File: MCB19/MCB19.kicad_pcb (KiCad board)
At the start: 2 copper layers, 88 parts, among them J401 USART, J402 DISABLE, J601 RJ45, J602 RJ45, J611 +BATT, J612 GND, J613 VBAT+, J614 VBAT-, Q601 IRFP260N, Q602 IRFP260N, U201 MCP2551-I/SN, U202 MCP2515-xSO, U401 ATMEGA328P-PU, U501 LM7805, U601 LM5104MNOPB, U602 INA211_DCK_6, U603 LM324, Y201 16MHz, Y401 16MHz

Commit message: Mudança nas trilhas para melhor funcionamento
Detalhes finais para a fabricação
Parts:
- removed C405: 100nF, Capacitor_SMD:C_0805_2012Metric_Pad1.15x1.40mm_HandSolder
- added R411: 100, Resistor_SMD:R_0805_2012Metric_Pad1.15x1.40mm_HandSolder, B.Cu at (158.8, 105.0)
- moved U602 2.51 mm to (90.7, 90.8)
- moved R401 2.09 mm to (160.9, 107.5)
- moved R610 1.69 mm to (86.8, 89.7), turned to 180 degrees
- moved R609 1.63 mm to (86.8, 92.2)
- moved TP209 0.49 mm to (166.4, 65.5)
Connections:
- J401 pad 4: Net-(C405-Pad2) -> /MCU/RESET
- U401 pad 1: /MCU/RESET -> Net-(R411-Pad2)
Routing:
- net GND: track 306.1 -> 332.5 mm, vias 20 -> 30
- net Net-(C405-Pad2): track 6.59 -> 0.00 mm
- net /MCU/RESET: track 12.1 -> 16.9 mm
- net Net-(R411-Pad2): track 0.00 -> 4.12 mm
- net Net-(J613-Pad1): track 67.9 -> 65.1 mm
- net Net-(R609-Pad2): track 4.69 -> 7.00 mm
- net /MCU/INALLL: track 71.7 -> 73.6 mm
- net Net-(C603-Pad1): track 29.0 -> 27.3 mm
- net Net-(C601-Pad2): track 108.6 -> 109.9 mm
- net +5V: track 339.9 -> 340.5 mm
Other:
- net class Shunt added: clearance 0.127, trace_width 0.508, via_dia 1.5, via_drill 0.8

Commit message: Final!!!
Pronto para fabricar
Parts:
- moved C606 34.3 mm to (94.1, 63.1), turned to 0 degrees
- moved R607 32.1 mm to (89.7, 63.1), turned to 180 degrees
- moved D604 29.4 mm to (91.5, 65.8), turned to 180 degrees
- moved U603 22.4 mm to (77.3, 116.0)
- moved R609 21.9 mm to (75.0, 110.7)
- moved R610 21.7 mm to (78.2, 109.7), turned to 270 degrees
- moved C607 7.16 mm to (109.5, 99.6)
- moved D605 7.16 mm to (106.9, 97.0)
- moved R608 7.16 mm to (109.5, 95.2)
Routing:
- net GND: track 332.5 -> 242.7 mm
- net Net-(J613-Pad1): track 65.1 -> 5.54 mm
- net Net-(C601-Pad2): track 109.9 -> 130.8 mm
- net +BATT: track 84.9 -> 71.3 mm
- net +5V: track 340.5 -> 350.1 mm, vias 8 -> 10
- net /MCU/INALLL: track 73.6 -> 79.6 mm
- net /driver/LM324A: track 80.8 -> 75.7 mm, vias 2 -> 0
- net Net-(R609-Pad2): track 7.00 -> 4.96 mm
- added copper zone on B.Cu, net Net-(J613-Pad1)

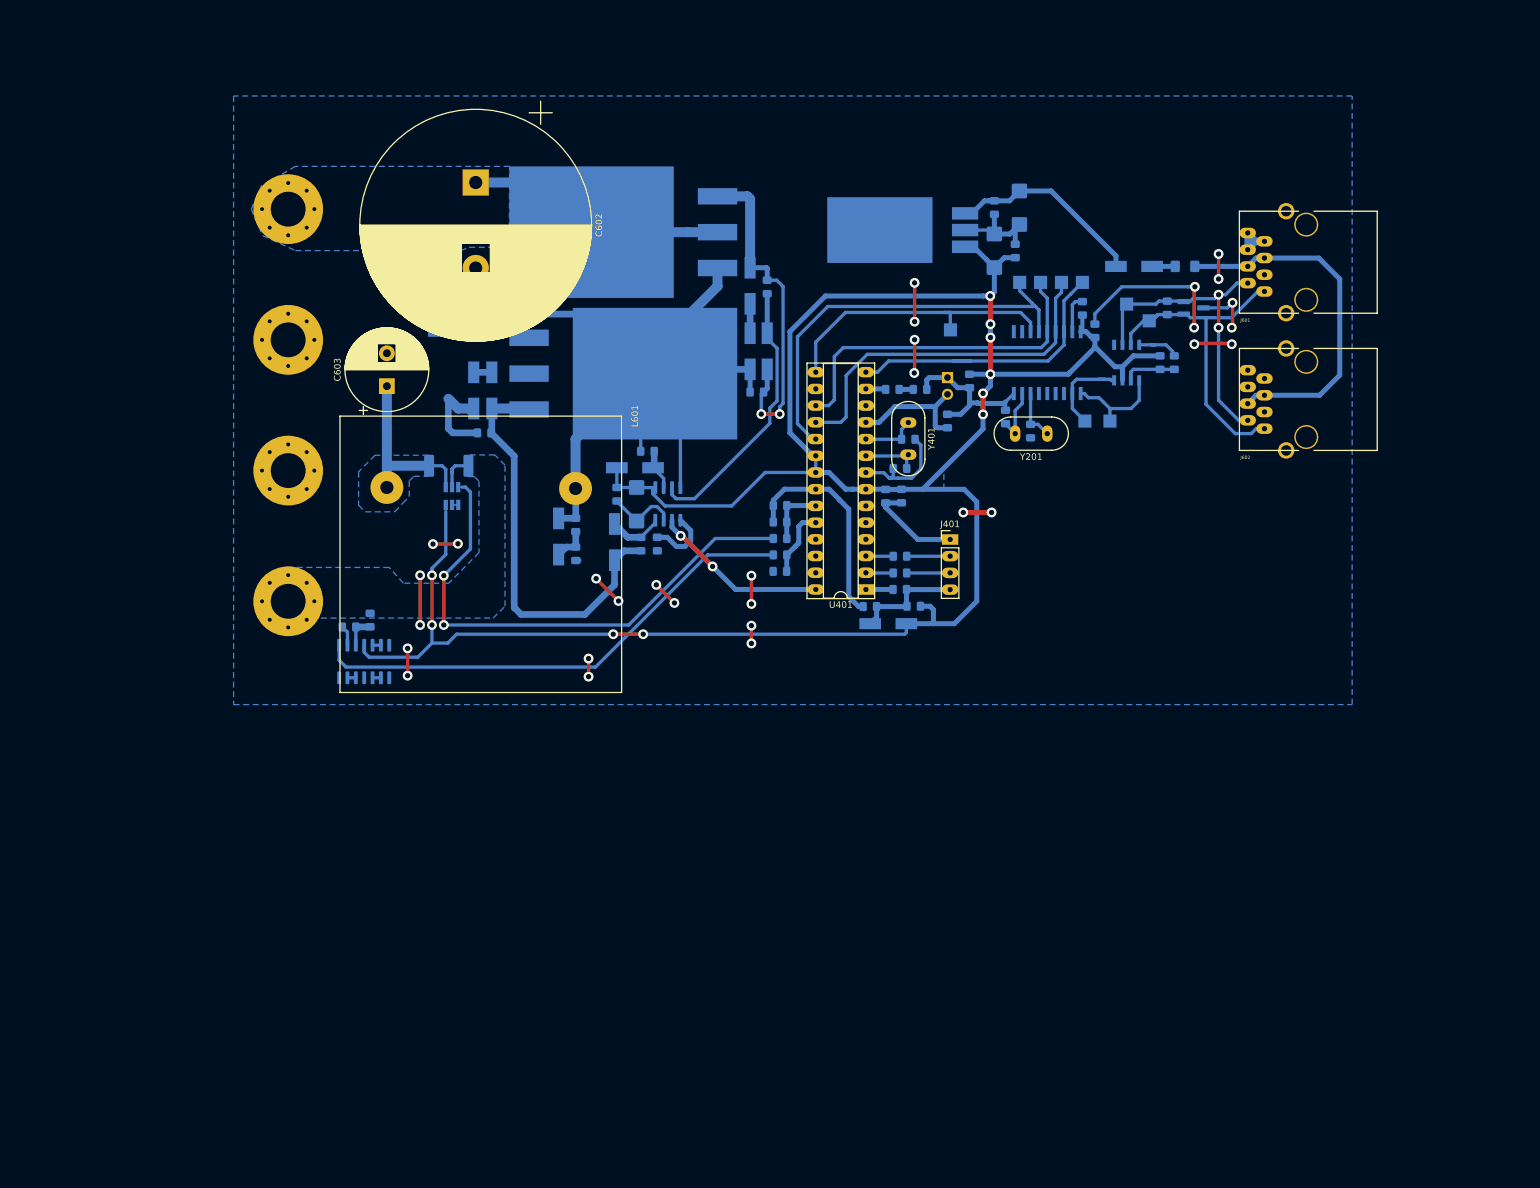
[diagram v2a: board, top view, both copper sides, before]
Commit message: Capacitor corrigido
Havia um capacitor com medidas erradas, que já foram corrigidas.
Para o protótipo já desenvolvido, não ha problemas pois há espaço para a correção.
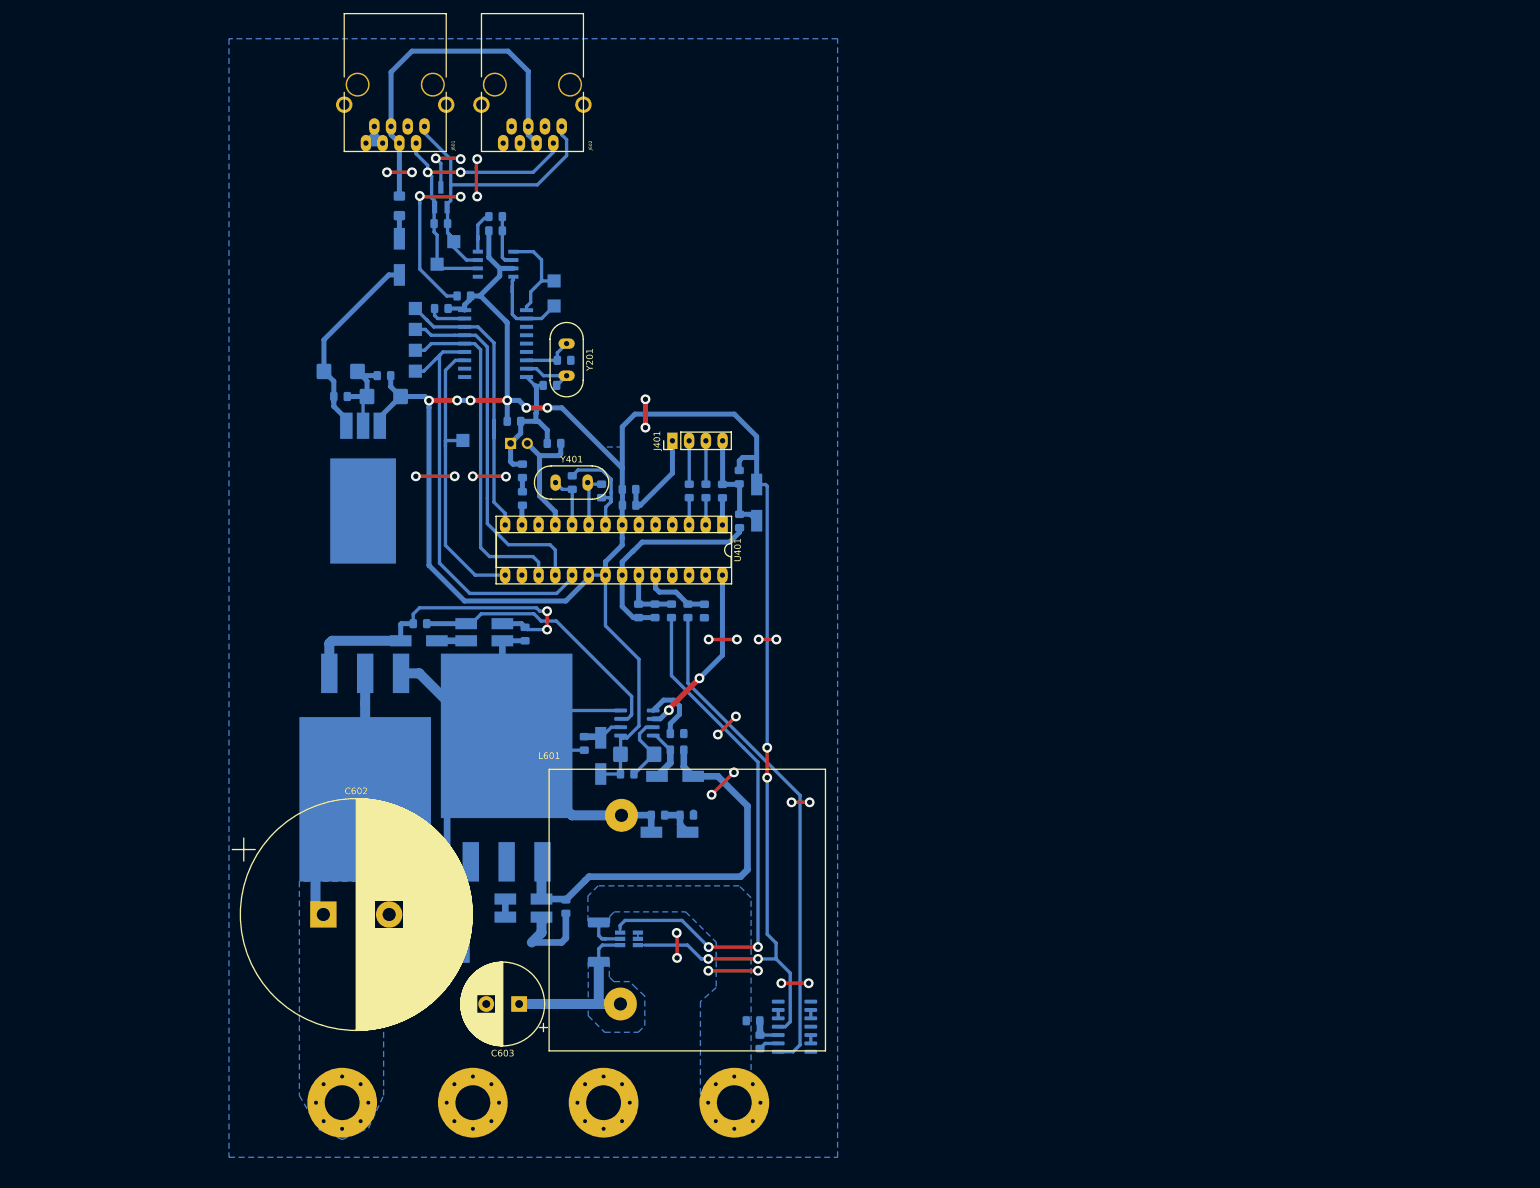
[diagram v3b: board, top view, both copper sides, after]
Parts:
- moved J611 136.0 mm to (74.0, 183.0), turned to 90 degrees
- moved J601 130.1 mm to (86.5, 34.6), turned to 180 degrees
- moved F501 119.8 mm to (82.7, 46.7), turned to 90 degrees
- moved J612 119.3 mm to (93.9, 183.0), turned to 90 degrees
- moved J602 116.3 mm to (107.4, 34.6), turned to 180 degrees
- moved D201 115.6 mm to (89.0, 45.4), turned to 90 degrees
- moved C602 112.2 mm to (71.2, 154.4), turned to 0 degrees
- moved D501 111.7 mm to (82.7, 54.5), turned to 90 degrees
- moved R201 111.1 mm to (89.0, 49.4), turned to 0 degrees
- moved J614 107.4 mm to (113.7, 183.0), turned to 270 degrees
- moved TP207 106.4 mm to (91.0, 52.1), turned to 90 degrees
- moved C501 106.1 mm to (73.8, 71.9), turned to 0 degrees
- moved R202 105.5 mm to (97.3, 48.3), turned to 0 degrees
- moved TP208 105.0 mm to (88.4, 55.6), turned to 90 degrees
- moved C502 103.4 mm to (73.8, 75.7), turned to 0 degrees
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
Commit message: New version
Detalhes
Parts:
- added C301: 1uF, Capacitor_Tantalum_SMD:CP_EIA-6032-20_AVX-F_Pad2.25x2.35mm_HandSolder, F.Cu at (205.0, 98.5)
- added C302: 100nF, Capacitor_SMD:C_0805_2012Metric_Pad1.15x1.40mm_HandSolder, F.Cu at (202.0, 105.8)
- added C303: 100nF, Capacitor_SMD:C_0805_2012Metric_Pad1.15x1.40mm_HandSolder, F.Cu at (192.6, 112.5)
- added C304: 1uF, Capacitor_Tantalum_SMD:CP_EIA-6032-20_AVX-F_Pad2.25x2.35mm_HandSolder, F.Cu at (194.2, 105.1)
- added D301: LL4148, Diode_SMD:D_MiniMELF_Handsoldering, F.Cu at (194.9, 97.7)
- added U301: LM7815, KicadZeniteSolarLibrary18:TO-220-3_Horizontal_TabDown_SMD, F.Cu at (180.8, 116.5)
- Q601, Q602: footprint KicadZeniteSolarLibrary18:TO-247-3_Horizontal_TabDown_SMD -> Package_TO_SOT_THT:TO-247-3_Vertical
- U501: value LM7805 -> LM7815
- moved J613 178.4 mm to (44.8, 28.4), turned to 90 degrees
- moved U603 169.7 mm to (35.6, 39.9), turned to 180 degrees
- moved R609 167.0 mm to (40.9, 37.6), turned to 270 degrees
- moved J614 162.3 mm to (64.6, 28.4), turned to 90 degrees
- moved R610 160.5 mm to (41.9, 40.8), turned to 180 degrees
- moved J611 157.6 mm to (104.3, 28.4), turned to 270 degrees
- moved J612 154.9 mm to (84.5, 28.4), turned to 270 degrees
- moved J602 146.7 mm to (71.0, 176.7), turned to 0 degrees
- moved J601 142.2 mm to (91.8, 176.7), turned to 0 degrees
- moved C603 126.8 mm to (77.5, 43.4), turned to 0 degrees
- moved D201 120.6 mm to (89.3, 165.9), turned to 270 degrees
- moved U602 119.3 mm to (60.8, 53.2), turned to 0 degrees
- moved F501 118.7 mm to (95.7, 164.7), turned to 270 degrees
- moved R606 116.1 mm to (65.3, 52.8), turned to 90 degrees
- moved R202 115.8 mm to (81.0, 163.0), turned to 180 degrees
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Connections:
- C503 pad 1: +5V -> +15V
- C504 pad 1: +5V -> +15V
- C604 pad 1: +5V -> +15V
- C605 pad 1: +5V -> +15V
- D601 pad 2: +5V -> +15V
- U501 pad 3: +5V -> +15V
- U601 pad 1: +5V -> +15V

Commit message: Versão 2.0
Novas modificações, após confirmado, pode ser fabricada
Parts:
- C301, C302, C303, C304, D301: moved to B.Cu
- C501, C502, C503, C504, C601, C604, C605, C606, C607, D501, D601, D602, D603, D604, D605, DZ601, DZ602, DZ603, DZ604, J611, J612, J613, J614, R601, R602, R603, R604, R605, R607, R608, U501, U601: moved to F.Cu
- L601: footprint MCCplaca:Inductor_Nocoupled -> KicadZeniteSolarLibrary18:Inductor_Nocoupled
- Q601, Q602: footprint Package_TO_SOT_THT:TO-247-3_Vertical -> Package_TO_SOT_THT:TO-247-3_Horizontal_TabUp
- U301: value LM7815 -> LM7805; moved to B.Cu
- moved C301 166.9 mm to (53.5, 168.5), turned to 180 degrees
- moved C302 158.3 mm to (55.0, 164.5), turned to 180 degrees
- moved C304 157.4 mm to (48.5, 164.5)
- moved C303 156.0 mm to (47.0, 168.5)
- moved D301 148.7 mm to (62.5, 165.5), turned to 270 degrees
- moved U301 134.0 mm to (53.5, 158.2), turned to 180 degrees
- moved U603 98.4 mm to (131.0, 64.0), turned to 0 degrees
- moved R609 89.4 mm to (125.5, 66.5), turned to 90 degrees
- moved R610 85.1 mm to (123.0, 66.5), turned to 90 degrees
- moved J614 68.6 mm to (132.0, 41.0), turned to 0 degrees
- moved C603 67.8 mm to (119.5, 96.5), turned to 270 degrees
- moved U602 66.1 mm to (124.0, 72.5), turned to 180 degrees
- moved J613 62.4 mm to (105.8, 41.0), turned to 0 degrees
- moved R606 57.8 mm to (119.5, 73.0), turned to 270 degrees
- moved C607 57.4 mm to (108.0, 84.5), turned to 0 degrees
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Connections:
- C303 pad 1: /POWER SUPPLY/+15V_OUT -> +5V
- C304 pad 1: /POWER SUPPLY/+15V_OUT -> +5V
- U301 pad 3: /POWER SUPPLY/+15V_OUT -> +5V
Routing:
- net /MCU/INALLL: track 79.6 -> 193.6 mm, vias 2 -> 4
- net /driver/LM324A: track 75.7 -> 188.3 mm, vias 0 -> 4
- net +15V: track 0.00 -> 74.1 mm
- net +5V: track 350.1 -> 281.1 mm, vias 10 -> 2
- net +BATT: track 71.3 -> 4.52 mm, vias 0 -> 2
- net Net-(C501-Pad1): track 30.0 -> 74.6 mm
- net GND: track 242.7 -> 203.9 mm, vias 30 -> 16
- net Net-(C601-Pad2): track 130.8 -> 93.2 mm, vias 0 -> 2
- net Net-(D603-Pad2): track 52.4 -> 17.0 mm, vias 2 -> 0
- net Net-(D602-Pad2): track 64.2 -> 29.2 mm
- net /MCU/PWM: track 27.7 -> 56.4 mm, vias 2 -> 3
- net Net-(D603-Pad1): track 41.7 -> 17.2 mm
- net Net-(C301-Pad1): track 0.00 -> 23.0 mm
- net /CANBUS CONN/CAN_18V: track 54.3 -> 70.9 mm
- net (no net): track 0.00 -> 7.95 mm
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- added copper zone on F.Cu, net +BATT
- added copper zone on F.Cu, net GND
- added copper zone on B.Cu, net Net-(C601-Pad2)
- added copper zone on F.Cu, net Net-(C601-Pad2)
- added copper zone on F.Cu, net Net-(C603-Pad1)
- added copper zone on F.Cu, net Net-(J613-Pad1)
- removed copper zone on B.Cu, net +5V
